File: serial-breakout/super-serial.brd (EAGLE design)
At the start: 50.8 x 31.7 mm, 7 parts, among them X1 2510-, X2 D-SUB9-H2M09ST

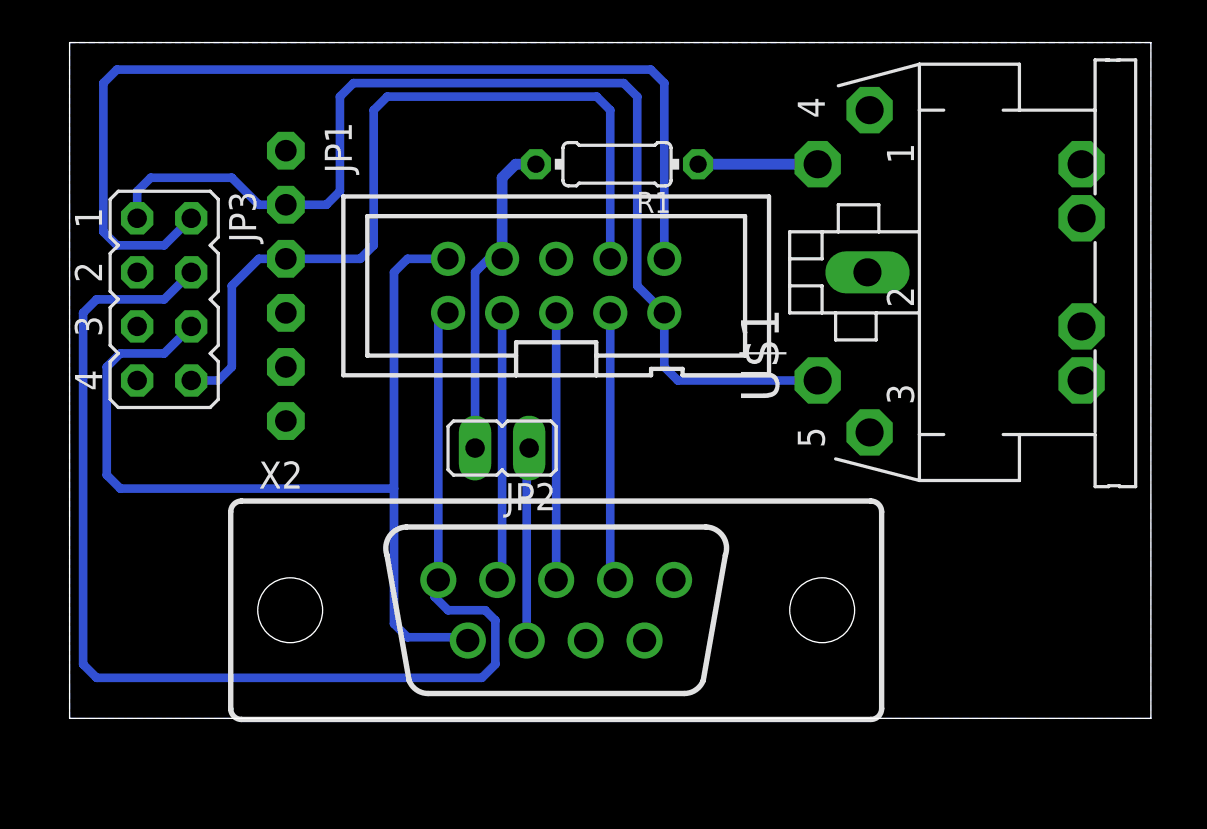
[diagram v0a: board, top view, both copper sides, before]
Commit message: add super serial
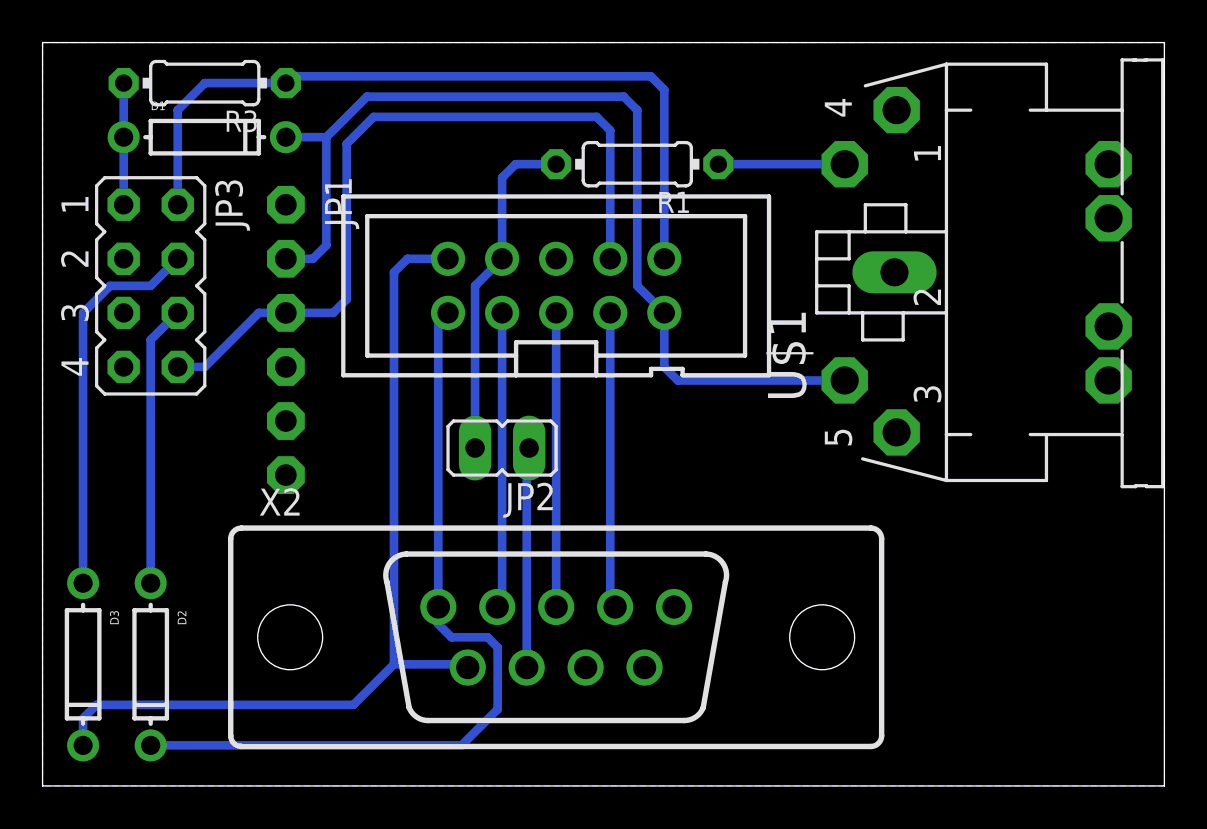
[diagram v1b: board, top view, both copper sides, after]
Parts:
- added D1, D2, D3: (no value), adafruit:DO-1N4148
- added R3: 10k, rcl:0204/7
- moved JP1 2.54 mm to (-7.62, 32.4)
- moved U$1 1.27 mm to (33.7, 35.6)
- moved X2 1.27 mm to (5.08, 18.4)
- moved R1 0.95 mm to (8.89, 40.6)
- moved JP3 0.90 mm to (-14.0, 34.9)
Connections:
- new net CH_PD: D2.A, JP3.6
- new net ESP-RX: D1.A, JP3.1, R3.2
- new net RST: D3.A, JP3.4
- net 3V3: now also R3.1
- net FIRE: now also D3.C; no longer JP3.6
- net TX: now also D1.C; no longer JP3.1
- net UP: now also D2.C; no longer JP3.4
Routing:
- net UP: track 61.3 -> 38.1 mm
- net RST: track 0.00 -> 18.2 mm
- net CH_PD: track 0.00 -> 13.2 mm
- net 3V3: track 47.0 -> 36.2 mm
- net ESP-RX: track 0.00 -> 5.72 mm
- net TX: track 51.5 -> 46.1 mm
- net FIRE: track 46.7 -> 41.7 mm
- net RX: track 38.4 -> 35.8 mm
- net RIGHT: track 12.6 -> 13.9 mm
- net LEFT: track 12.5 -> 13.8 mm
- net DOWN: track 12.6 -> 13.9 mm
- net 5V0': track 9.09 -> 10.4 mm
- net 5V0: track 15.4 -> 16.0 mm
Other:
- board size 50.8 x 31.7 mm -> 52.7 x 34.9 mm
